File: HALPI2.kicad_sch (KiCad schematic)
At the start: 0 parts

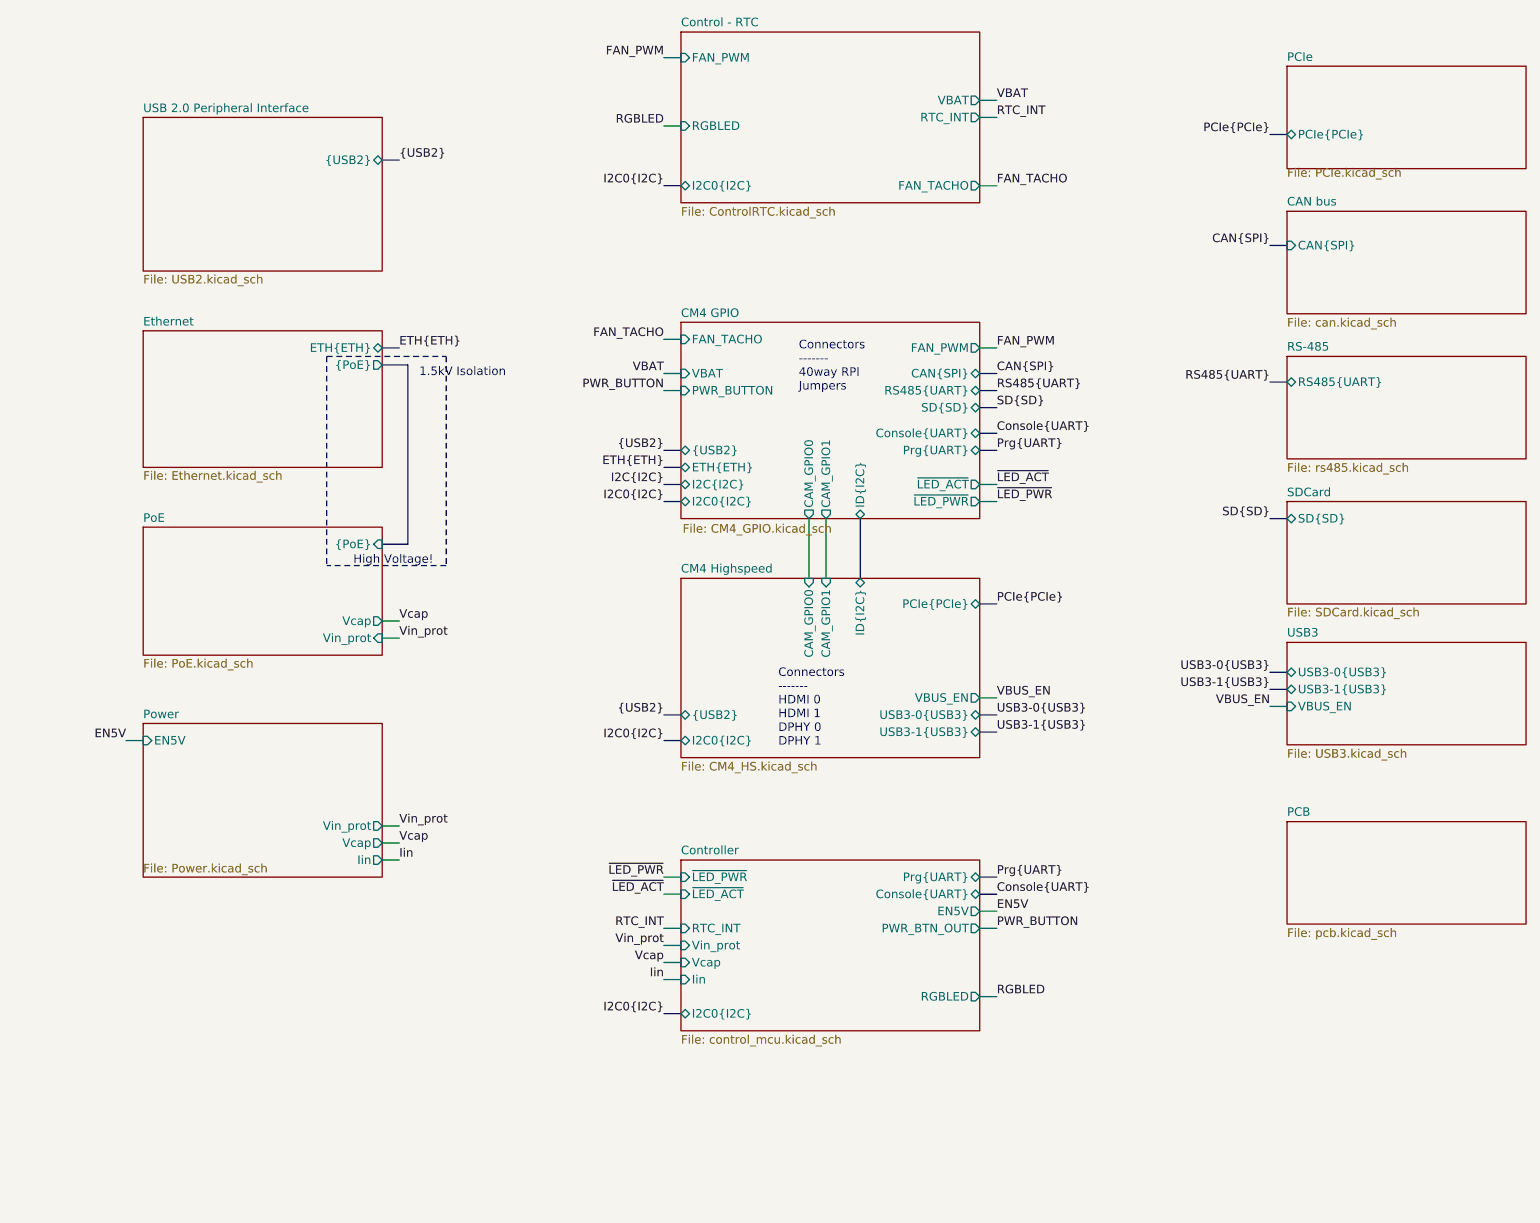
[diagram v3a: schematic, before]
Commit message: Partial trace layout, kick-ass custom rules
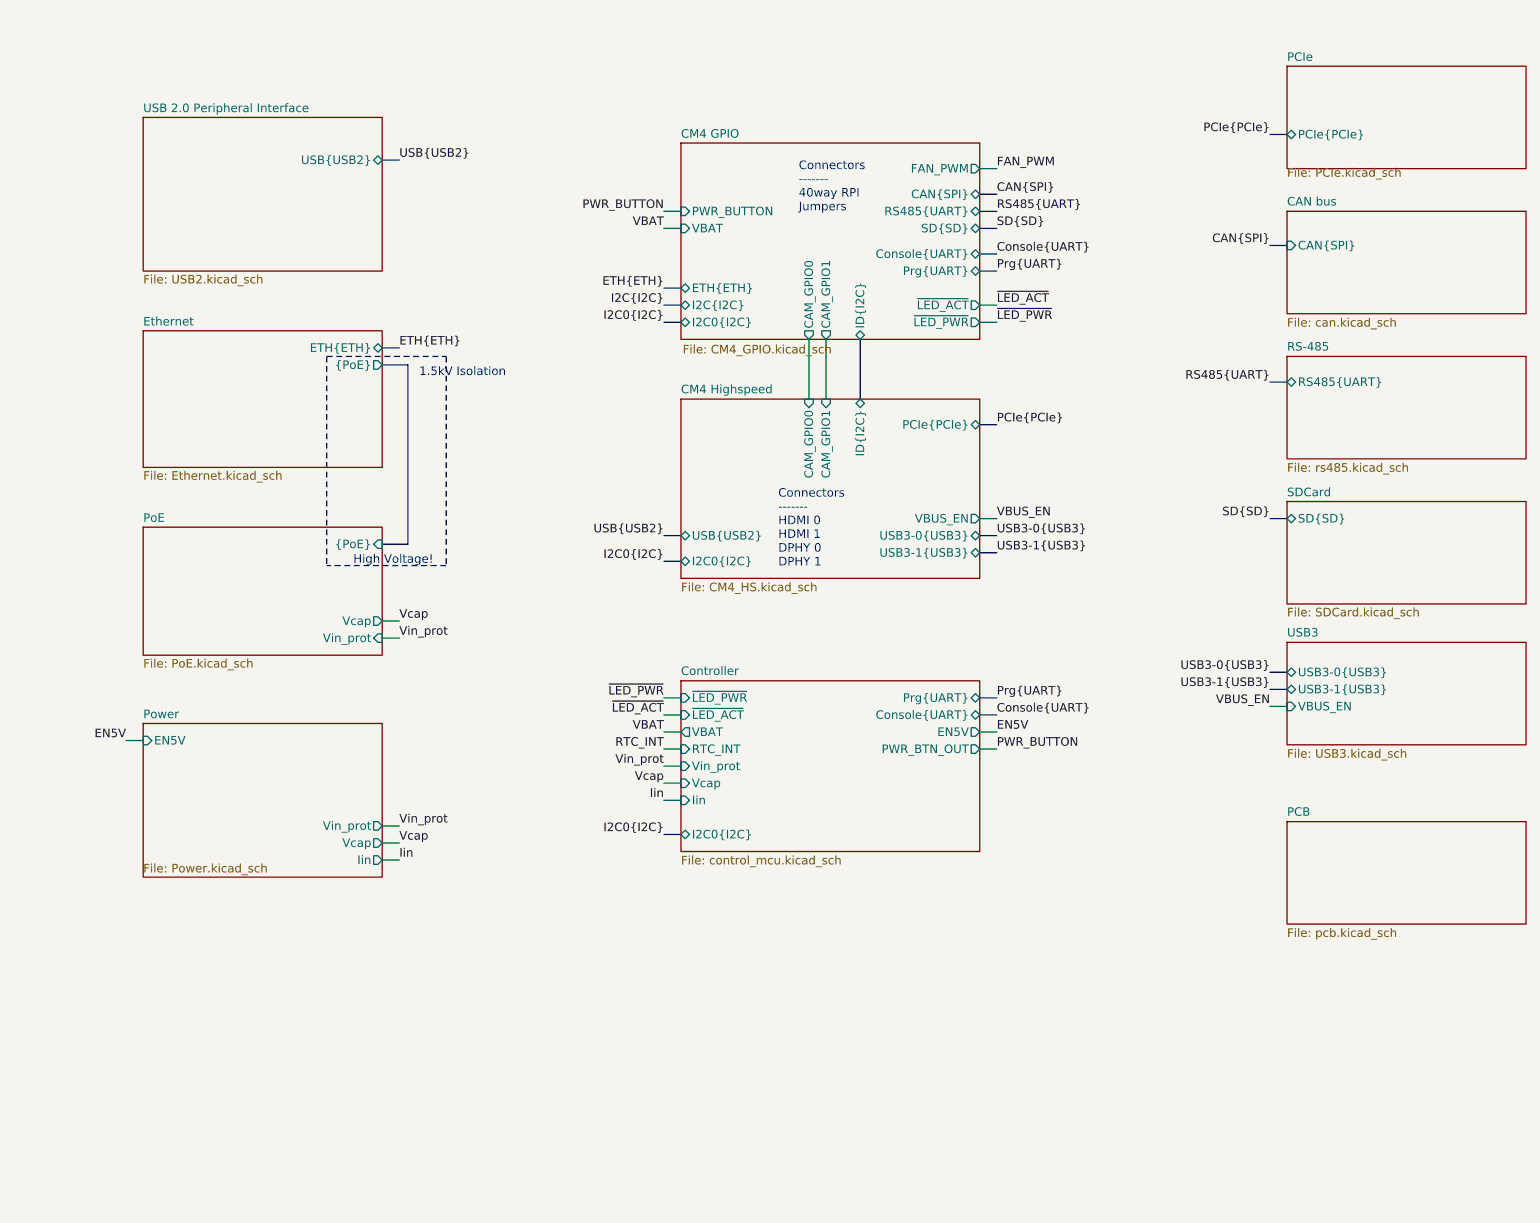
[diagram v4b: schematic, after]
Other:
- removed sheet Control - RTC
- sheet CM4 GPIO ports: added none; removed FAN_TACHO, {USB2}
- sheet CM4 Highspeed ports: added USB{USB2}; removed {USB2}
- sheet Controller ports: added VBAT; removed RGBLED
- sheet USB 2.0 Peripheral Interface ports: added USB{USB2}; removed {USB2}

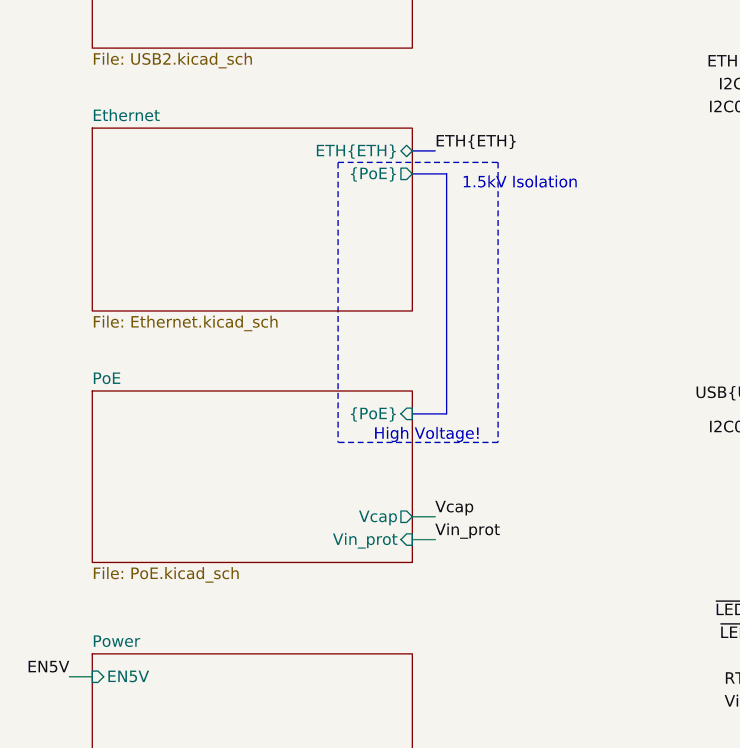
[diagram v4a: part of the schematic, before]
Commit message: Remove PoE support
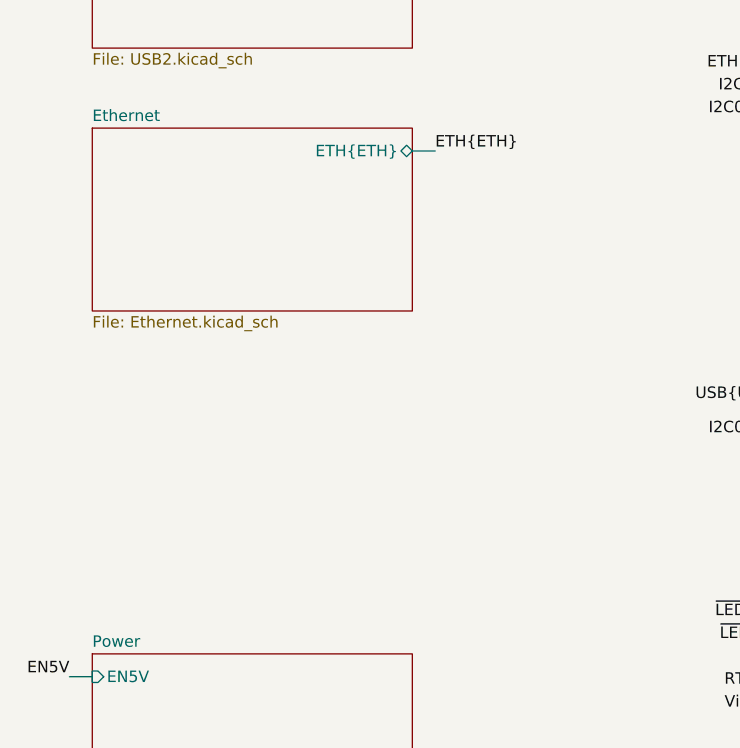
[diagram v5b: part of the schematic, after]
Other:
- removed sheet PoE
- sheet Ethernet ports: added none; removed {PoE}
- note removed: "1.5kV Isolation"
- note removed: "High Voltage!"
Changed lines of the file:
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@@
-	(bus
-		(pts
-			(xy 71.12 93.98) (xy 74.93 93.98)
-		)
-		(stroke
-			(width 0)
-			(type solid)
-		)
-	)
 	(bus
 		(pts
@@
 		)
 	)
-	(polyline
-		(pts
-			(xy 62.865 66.04) (xy 62.865 97.155)
-		)
-		(stroke
-			(width 0)
-			(type dash)
-		)
-	)
 	(wire
 		(pts
@@
 		)
 	)
-	(polyline
-		(pts
-			(xy 80.645 97.155) (xy 62.865 97.155)
-		)
-		(stroke
-			(width 0)
-			(type dash)
-		)
-	)
-	(bus
-		(pts
-			(xy 74.93 67.31) (xy 74.93 93.98)
-		)
-		(stroke
-			(width 0)
-			(type solid)
-		)
-	)
 	(wire
 		(pts
@@
 		)
 	)
-	(polyline
-		(pts
-			(xy 62.865 66.04) (xy 80.645 66.04)
-		)
-		(stroke
-			(width 0)
-			(type dash)
-		)
-	)
 	(bus
 		(pts
@@
 	(bus
 		(pts
-			(xy 71.12 67.31) (xy 74.93 67.31)
-		)
-		(stroke
-			(width 0)
-			(type solid)
-		)
-	)
-	(bus
-		(pts
 			(xy 203.2 115.57) (xy 205.74 115.57)
 		)
@@
 		)
 	)
-	(wire
-		(pts
-			(xy 71.12 105.41) (xy 73.66 105.41)
-		)
-		(stroke
-			(width 0)
-			(type default)
-		)
-	)
-	(wire
-		(pts
-			(xy 73.66 107.95) (xy 71.12 107.95)
-		)
-		(stroke
-			(width 0)
-			(type default)
-		)
-	)
 	(bus
 		(pts
@@
 			(width 0)
 			(type default)
-		)
-	)
-	(polyline
-		(pts
-			(xy 80.645 66.04) (xy 80.645 97.155)
-		)
-		(stroke
-			(width 0)
-			(type dash)
 		)
 	)
@@
 		)
 	)
-	(text "1.5kV Isolation"
-		(exclude_from_sim no)
-		(at 89.535 69.215 0)
-		(effects
-			(font
-				(size 1.27 1.27)
-			)
-			(justify right bottom)
-		)
-	)
-	(text "High Voltage!"
-		(exclude_from_sim no)
-		(at 78.74 97.155 0)
-		(effects
-			(font
-				(size 1.27 1.27)
-			)
-			(justify right bottom)
-		)
-	)
 	(label "EN5V"
 		(at 33.02 123.19 180)
@@
 		)
 	)
-	(label "Vin_prot"
-		(at 73.66 107.95 0)
-		(effects
-			(font
-				(size 1.27 1.27)
-			)
-			(justify left bottom)
-		)
-	)
 	(label "EN5V"
 		(at 162.56 121.92 0)
@@
 			)
 			(justify right bottom)
-		)
-	)
-	(label "Vcap"
-		(at 73.66 105.41 0)
-		(effects
-			(font
-				(size 1.27 1.27)
-			)
-			(justify left bottom)
 		)
 	)
@@
 			)
 		)
-		(pin "{PoE}" output
-			(at 71.12 67.31 0)
-			(effects
-				(font
-					(size 1.27 1.27)
-				)
-				(justify right)
-			)
-		)
 		(instances
 			(project "HALPI2"
@@
 				)
 			)
-		)
-	)
-	(sheet
-		(at 35.56 91.44)
-		(size 35.56 19.05)
-		(stroke
-			(width 0)
-			(type solid)
-			(color 132 0 132 1)
-		)
-		(fill
-			(color 255 255 255 0.0000)
-		)
-		(property "Sheetname" "PoE"
-			(at 35.56 90.8041 0)
-			(effects
-				(font
-					(size 1.27 1.27)
-				)
-				(justify left bottom)
-			)
-		)
-		(property "Sheetfile" "PoE.kicad_sch"
-			(at 35.56 110.9989 0)
-			(effects
-				(font
-					(size 1.27 1.27)
-				)
-				(justify left top)
-			)
-		)
-		(pin "{PoE}" input
-			(at 71.12 93.98 0)
-			(effects
-				(font
-					(size 1.27 1.27)
-				)
-				(justify right)
-			)
-		)
-		(pin "Vin_prot" input
-			(at 71.12 107.95 0)
-			(effects
-				(font
-					(size 1.27 1.27)
-				)
-				(justify right)
-			)
-		)
-		(pin "Vcap" output
-			(at 71.12 105.41 0)
-			(effects
-				(font
-					(size 1.27 1.27)
-				)
-				(justify right)
-			)
-		)
-		(instances
-			(project "HALPI2"
-				(path "/abc482bd-3f17-4d35-80db-1da3dcdb5c27"
-					(page "11")
-				)
-			)

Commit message: A big part of layout and routing done
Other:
- sheet CM4 GPIO ports: added RS485{RS485}; removed RS485{UART}
- sheet RS-485 ports: added RS485{RS485}; removed RS485{UART}
- sheet USB3 ports: added I2C0{I2C}; removed none

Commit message: Route more traces
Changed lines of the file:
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@@
 	(bus
 		(pts
-			(xy 203.2 49.53) (xy 205.74 49.53)
-		)
-		(stroke
-			(width 0)
-			(type default)
-		)
-	)
-	(wire
-		(pts
-			(xy 203.2 118.11) (xy 205.74 118.11)
+			(xy 203.2 50.8) (xy 205.74 50.8)
+		)
+		(stroke
+			(width 0)
+			(type default)
+		)
+	)
+	(wire
+		(pts
+			(xy 203.2 123.825) (xy 205.74 123.825)
 		)
 		(stroke
@@
 	(bus
 		(pts
-			(xy 203.2 90.17) (xy 205.74 90.17)
+			(xy 203.2 93.98) (xy 205.74 93.98)
 		)
 		(stroke
@@
 	(bus
 		(pts
-			(xy 203.2 120.65) (xy 205.74 120.65)
+			(xy 203.2 126.365) (xy 205.74 126.365)
 		)
 		(stroke
@@
 	(bus
 		(pts
-			(xy 203.2 115.57) (xy 205.74 115.57)
+			(xy 203.2 121.285) (xy 205.74 121.285)
 		)
 		(stroke
@@
 	(bus
 		(pts
-			(xy 203.2 69.85) (xy 205.74 69.85)
+			(xy 203.2 72.39) (xy 205.74 72.39)
 		)
 		(stroke
@@
 	(bus
 		(pts
-			(xy 203.2 113.03) (xy 205.74 113.03)
+			(xy 203.2 118.745) (xy 205.74 118.745)
 		)
 		(stroke
@@
 	)
 	(label "SD{SD}"
-		(at 203.2 90.17 180)
+		(at 203.2 93.98 180)
 		(effects
 			(font
@@
 	)
 	(label "CAN{SPI}"
-		(at 203.2 49.53 180)
+		(at 203.2 50.8 180)
 		(effects
 			(font
@@
 	)
 	(label "RS485{RS485}"
-		(at 203.2 69.85 180)
+		(at 203.2 72.39 180)
 		(effects
 			(font
@@
 	)
 	(label "VBUS_EN"
-		(at 203.2 118.11 180)
+		(at 203.2 123.825 180)
 		(effects
 			(font
@@
 	)
 	(label "USB3-1{USB3}"
-		(at 203.2 115.57 180)
+		(at 203.2 121.285 180)
 		(effects
 			(font
@@
 	)
 	(label "USB3-0{USB3}"
-		(at 203.2 113.03 180)
+		(at 203.2 118.745 180)
 		(effects
 			(font
@@
 	)
 	(label "I2C0{I2C}"
-		(at 203.2 120.65 180)
+		(at 203.2 126.365 180)
 		(effects
 			(font
@@
 	)
 	(sheet
-		(at 205.74 66.04)
+		(at 205.74 68.58)
 		(size 35.56 15.24)
 		(exclude_from_sim no)
@@
 		)
 		(property "Sheetname" "RS-485"
-			(at 205.74 65.3284 0)
+			(at 205.74 67.8684 0)
 			(effects
 				(font
@@
 		)
 		(property "Sheetfile" "rs485.kicad_sch"
-			(at 205.74 81.8646 0)
+			(at 205.74 84.4046 0)
 			(effects
 				(font
@@
 		)
 		(pin "RS485{RS485}" bidirectional
-			(at 205.74 69.85 180)
+			(at 205.74 72.39 180)
 			(effects
 				(font
@@
 	)
 	(sheet
-		(at 205.74 44.45)
+		(at 205.74 45.72)
 		(size 35.56 15.24)
 		(exclude_from_sim no)
@@
 		)
 		(property "Sheetname" "CAN bus"
-			(at 205.74 43.7384 0)
+			(at 205.74 45.0084 0)
 			(effects
 				(font
@@
 		)
 		(property "Sheetfile" "can.kicad_sch"
-			(at 205.74 60.2746 0)
+			(at 205.74 61.5446 0)
 			(effects
 				(font
@@
 		)
 		(pin "CAN{SPI}" input
-			(at 205.74 49.53 180)
+			(at 205.74 50.8 180)
 			(effects
 				(font
@@
 	)
 	(sheet
-		(at 205.74 87.63)
+		(at 205.74 91.44)
 		(size 35.56 15.24)
 		(exclude_from_sim no)
@@
 		)
 		(property "Sheetname" "SDCard"
-			(at 205.74 86.9941 0)
+			(at 205.74 90.8041 0)
 			(effects
 				(font
@@
 		)
 		(property "Sheetfile" "SDCard.kicad_sch"
-			(at 205.74 103.3789 0)
+			(at 205.74 107.1889 0)
 			(effects
 				(font
@@
 		)
 		(pin "SD{SD}" bidirectional
-			(at 205.74 90.17 180)
+			(at 205.74 93.98 180)
 			(effects
 				(font
@@
 	)
 	(sheet
-		(at 205.74 108.585)
+		(at 205.74 114.3)
 		(size 35.56 15.24)
 		(exclude_from_sim no)
@@
 		)
 		(property "Sheetname" "USB3"
-			(at 205.74 107.8734 0)
+			(at 205.74 113.5884 0)
 			(effects
 				(font
@@
 		)
 		(property "Sheetfile" "USB3.kicad_sch"
-			(at 205.74 124.4096 0)
+			(at 205.74 130.1246 0)
 			(effects
 				(font
@@
 		)
 		(pin "USB3-0{USB3}" bidirectional
-			(at 205.74 113.03 180)
+			(at 205.74 118.745 180)
 			(effects
 				(font
@@
 		)
 		(pin "USB3-1{USB3}" bidirectional
-			(at 205.74 115.57 180)
+			(at 205.74 121.285 180)
 			(effects
 				(font
@@
 		)
 		(pin "VBUS_EN" input
-			(at 205.74 118.11 180)
+			(at 205.74 123.825 180)
 			(effects
 				(font
@@
 		)
 		(pin "I2C0{I2C}" bidirectional
-			(at 205.74 120.65 180)
+			(at 205.74 126.365 180)
 			(effects
 				(font
@@
 	)
 	(sheet
-		(at 205.74 135.255)
+		(at 205.74 138.43)
 		(size 35.56 15.24)
 		(exclude_from_sim no)
@@
 		)
 		(property "Sheetname" "PCB"
-			(at 205.74 134.5434 0)
+			(at 205.74 137.7184 0)
 			(effects
 				(font
@@
 		)
 		(property "Sheetfile" "pcb.kicad_sch"
-			(at 205.74 151.0796 0)
-			(effects
-				(font
+			(at 205.74 154.2546 0)
+			(effects
+				(font
